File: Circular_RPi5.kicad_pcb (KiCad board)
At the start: 6 copper layers, 80 x 80 mm, 32 parts, among them J1 USB3_A, J2 Conn_01x22, J3 GPIO Pins, J4 USB_C, J5 HDMI_D_1.4, J7 RJ45_RB1-125B8G1A, U1 USBLC, U2 USBLC, U3 USBLC, U4 USBLC, U5 USBLC, U6 TPD, U7 TPS, U8 USBLC

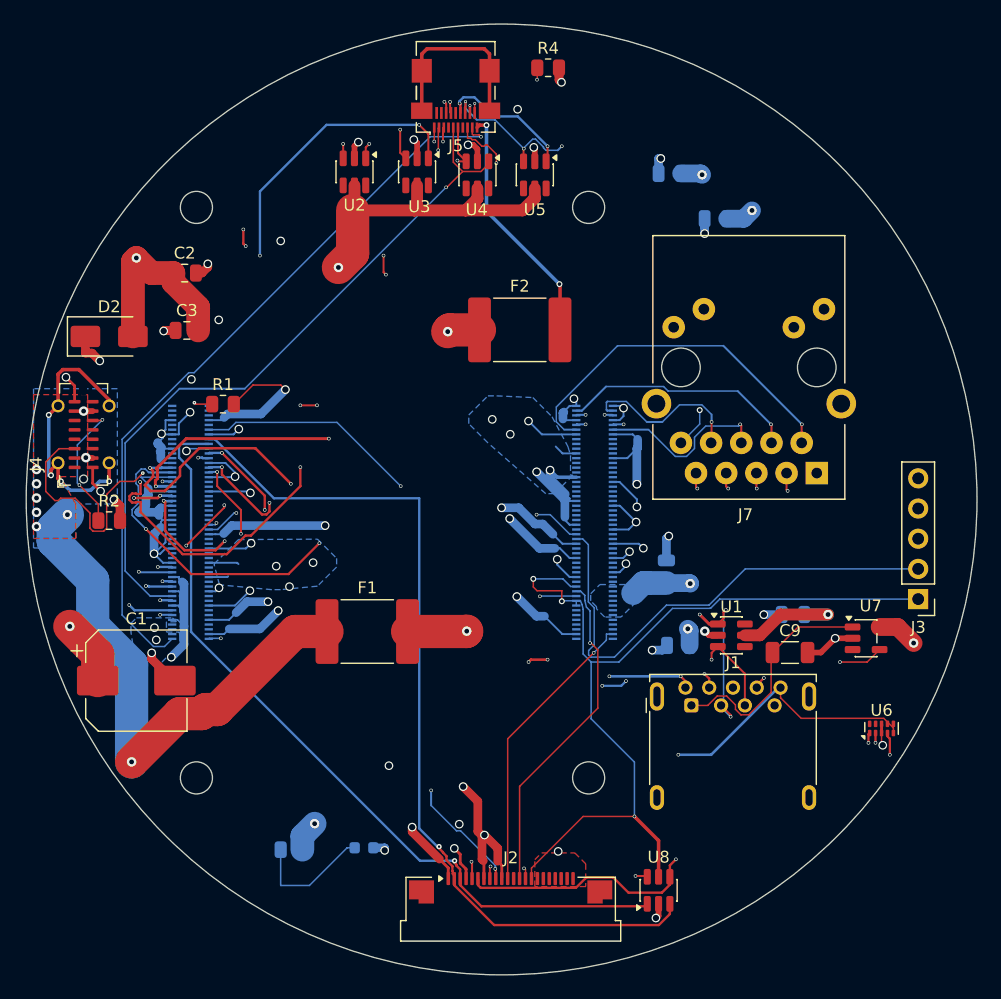
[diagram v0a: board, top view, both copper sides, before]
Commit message: Scope the 5A width rule to the real high-current path; DRC now clean
DRC: 39 violations -> 1 (the harmless "CM5IO library not configured locally"
note). 0 unconnected pads, 0 footprint errors.

Root cause: the 2.5mm minimum was applied to the whole +5V net, but +5V
distribution on this board is plane-based -- a 4614 mm2 pour on In3.Cu with 12
0.8mm/0.4mm stitching vias. Almost all +5V surface copper is therefore a short
local branch, not a current path. Tracing all 37 flagged segments to what they
actually feed:

   15 segs @1.0mm  U1..U5 ESD diode VBUS pins   leakage, microamps
  ~13 segs         C2..C8 decoupling stubs      AC only, no DC path
    1 seg  @2.0mm  D2 TVS                       leakage, microamps
    2 segs @2.0mm  R3 power LED                 9 mA
    3 segs @1.5mm  U7 USB load switch IN        ~1.5A -> 1.3 C rise, fine
    1 seg  @2.0mm  CM5 +5V feed                 up to 5A -> 12.2 C rise, fine

So 36 of 37 were false alarms: the rule was demanding 2.5mm of a trace biasing
an ESD diode. DRC has no topology, so a net-wide width rule cannot distinguish
the trunk from a milliamp stub.

Fix: two named rule areas "HC_5V" now mark the only two stretches of surface
copper that carry the full current -- F1's output to its plane via, and the
plane via feeding the CM5 +5V pins -- and the width constraint is scoped to
them via A.insideArea('HC_5V'). Area B was trimmed to y<=106.5 so it stops
catching C8's decoupling stub. Minimum set to 2.0mm (4.59A at 10 C rise on this
stackup) with 2.8mm as the optimum.

One genuine weakness was found and fixed while tracing: the narrowest link in
the CM5 +5V feed chain was 1.5mm, which at a full 5A would run a 19.5 C rise.
Widened to the maximum the local clearance allows -- 2.557mm and 2.800mm --
bringing it to about 8 C. Both widths were computed from actual distance to
every non-same-net pad, track and via on the layer, so no clearance regression.

Co-Authored-By: Claude Opus 5 <noreply@anthropic.com>
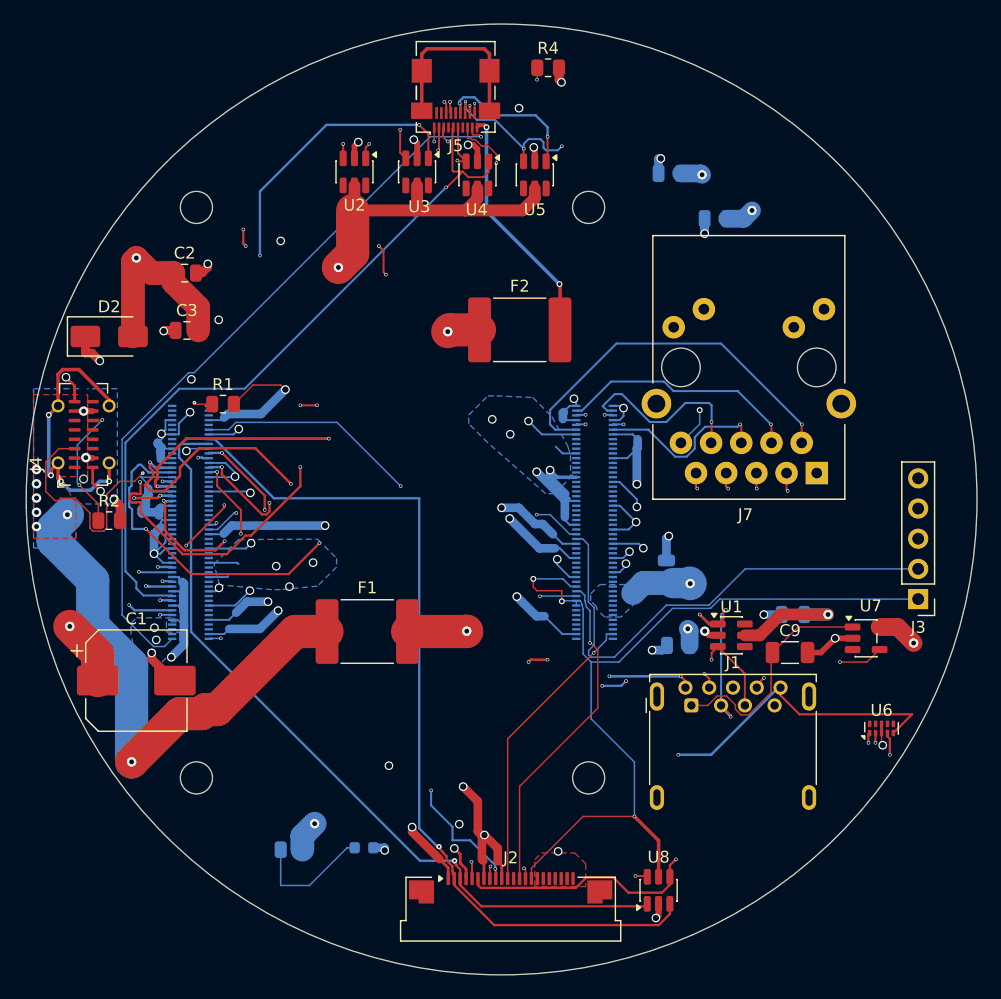
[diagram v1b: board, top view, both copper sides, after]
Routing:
- net /SSRX-: track 85.9 -> 89.4 mm
- net /HDMI0_TX0_P: track 60.2 -> 61.7 mm
- net /Ethernet_Pair3_P: track 14.1 -> 15.5 mm
- net /SSRX+: track 119.0 -> 120.3 mm
- net /Ethernet_Pair0_P: track 30.3 -> 31.5 mm
- net /HDMI0_TX0_N: track 53.3 -> 54.3 mm
- net /MIPI0_C_P: track 44.9 -> 45.5 mm
- net /HDMI0_TX2_N: track 58.3 -> 58.9 mm

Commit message: Final layout: DRC clean, J1 placed on-board, cleared for prototype fabrication
Sargunjit's interactive routing pass clears the remaining width violations and
places J1 (USB3 Type-A) fully inside the board outline.

Verification for this state:
- DRC: 1 violation, and it is the "CM5IO footprint library not configured"
  note -- a local KiCad library-table issue on this machine, not a board defect.
- 0 unconnected pads. 0 DRC exclusions. No safety-critical rule downgraded to
  warning or ignore (clearance, shorting_items, copper_edge_clearance,
  hole_clearance, unconnected_items, track_width, solder_mask_bridge all error).
- 0 vias inside SMD pads. 0 pads outside or within 0.2mm of the board edge.
- Gerbers (28 files) and drill export generate cleanly.
- Schematic parity: 21 items, all cosmetic silkscreen Value truncation or pads
  that are legitimately unconnected in the schematic.

J1 sits with +3.97mm pad margin to the edge; the only thing crossing the outline
is 0.10mm of F.Courtyard, an annotation layer, which is normal for an
edge-facing connector. The ten apparent footprint-body overlaps are Module1
(bottom side, flipped) against top-side parts -- opposite faces, no conflict.

All fixes from the design review confirmed still present: GPIO_VREF tied to
+3.3V, USB2 D+/D- moved to CM5 pins 134/136 so they share the USB3-0 controller,
J1 shield and GND_DRAIN both to GND, U8 MIPI ESD inline, C9 22uF on USB VBUS,
Ethernet pairs 2/3 wired, F1/F2 as real 5A PTCs, J7 as a genuine Gigabit
magjack. VBUS entry is 26.25 + 58.68 mm2 of zone with 9 vias (~8.6A against a
5A requirement); +5V rides a 4614 mm2 plane on In3.Cu.

Outstanding risk, deliberately accepted for a prototype run and NOT a DRC error:
eight differential pairs (USB3 TX/RX, HDMI TX0/TX1/TX2, MIPI D0/D1/CLK) are
routed as two independent traces rather than coupled pairs, giving roughly
147 ohm differential against a 90/100 ohm target. Expect USB3 to fall back to
USB 2.0 rather than negotiate 5 Gbps; MIPI is 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
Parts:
- moved U8 25.9 mm to (129.0, 129.8)
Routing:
- net /MIPI0_D1_P: track 88.1 -> 113.3 mm
- net /+3.3V: track 76.9 -> 89.7 mm, vias 3 -> 5
- net /MIPI0_D0_N: track 74.4 -> 62.3 mm
- net /MIPI0_D0_P: track 67.6 -> 63.3 mm
- net GND: track 243.4 -> 246.0 mm
- net /MIPI0_D1_N: track 61.0 -> 62.6 mm, vias 4 -> 3
